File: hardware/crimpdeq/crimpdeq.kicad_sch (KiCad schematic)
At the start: 52 parts, among them J2 USB4105-GF-A, Q1 S8550, Q2 DMG3415U, SW1 SW_Push, SW2 SW_Push, U1 ESP32-C3-MINI-1, U2 MCP73831T-2ACI/OT, U3 HX711, U4 Rust_Board, U6 SY8088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

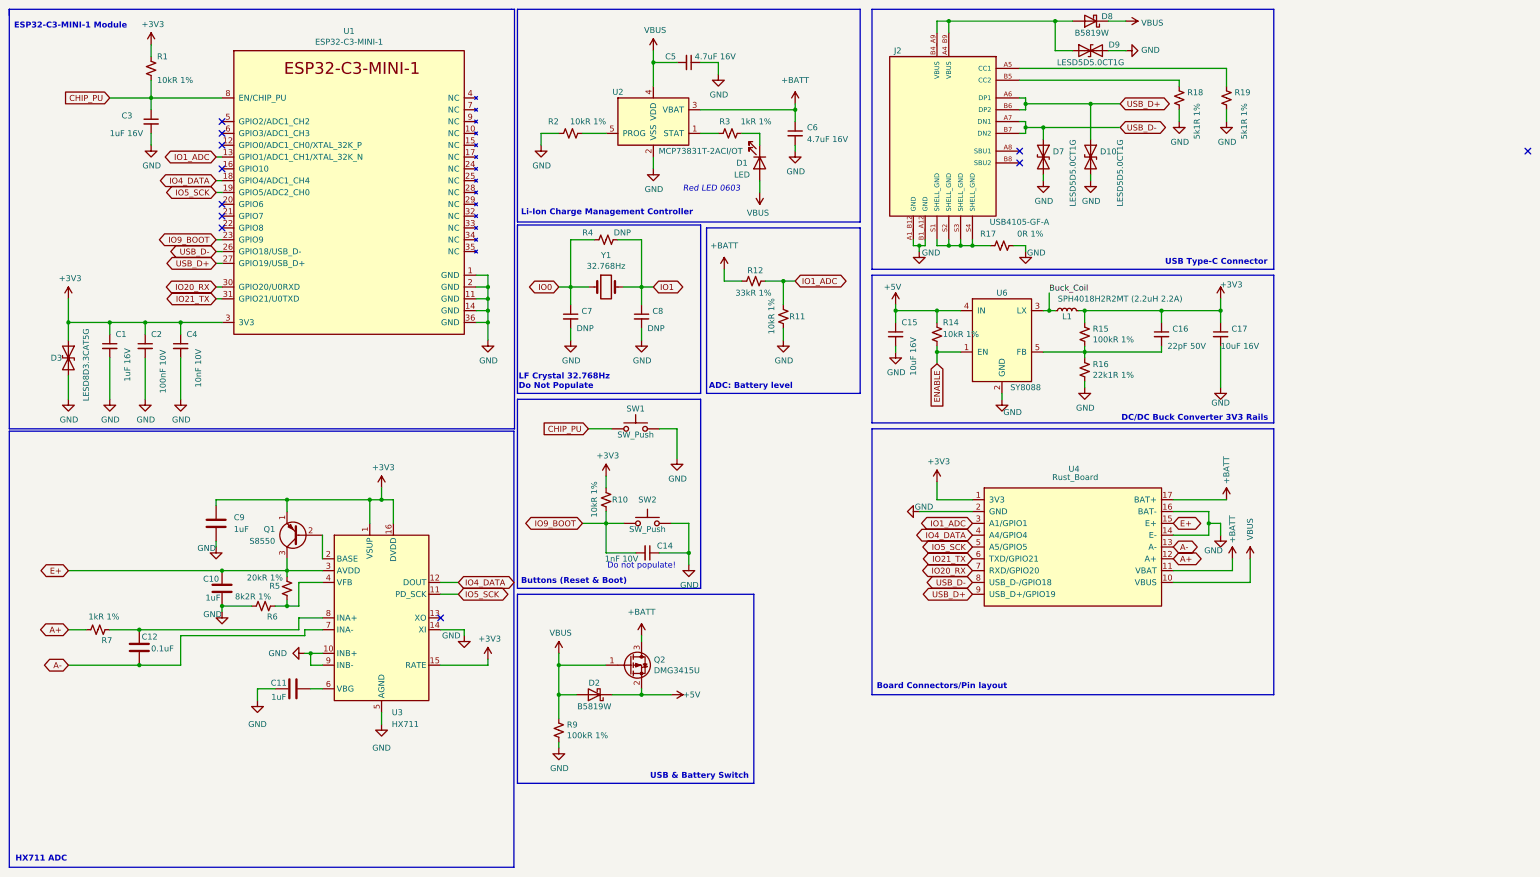
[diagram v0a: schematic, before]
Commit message: Update hx711 schematic according to the datasheet (#35)
* pcb: Update hx711 schematic according to the datasheet

* feat: Generate gerber files

* feat: Regenerate production files
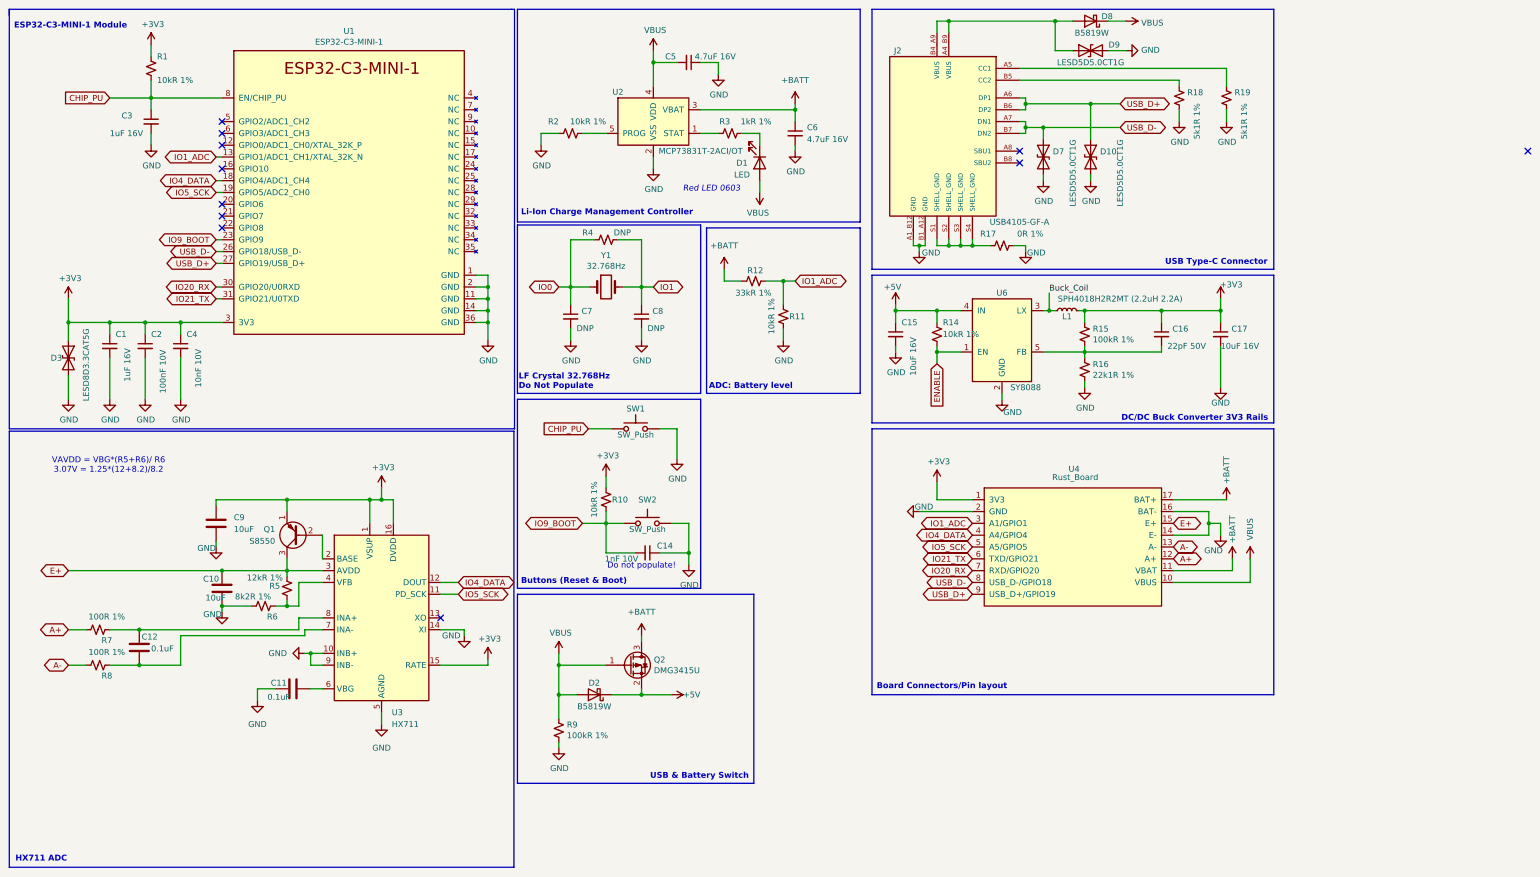
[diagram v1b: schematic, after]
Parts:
- added R8: 100R 1%, Resistor_SMD:R_0402_1005Metric, symbol Device:R_Small_US
- C10, C9: value 1uF -> 10uF
- C11: value 1uF -> 0.1uF
- R5: value 20kR 1% -> 12kR 1%
- R7: value 1kR 1% -> 100R 1%
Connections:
- net A-: now also R8.2; no longer C12.2, U3.7 (INA-)
- new net: C12.2, R8.1, U3.7 (INA-)
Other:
- note added: "VAVDD = VBG*(R5+R6)/ R6 3.07V = 1.25*(12+8.2)/8.2"
